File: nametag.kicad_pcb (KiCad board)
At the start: 2 copper layers, 180 x 54 mm, 116 parts, among them P1 ISP, Q1 2N7002, Q2 2N7002, Q3 2N7002, Q4 2N7002, Q5 2N7002, U1 ATTINY13-SS

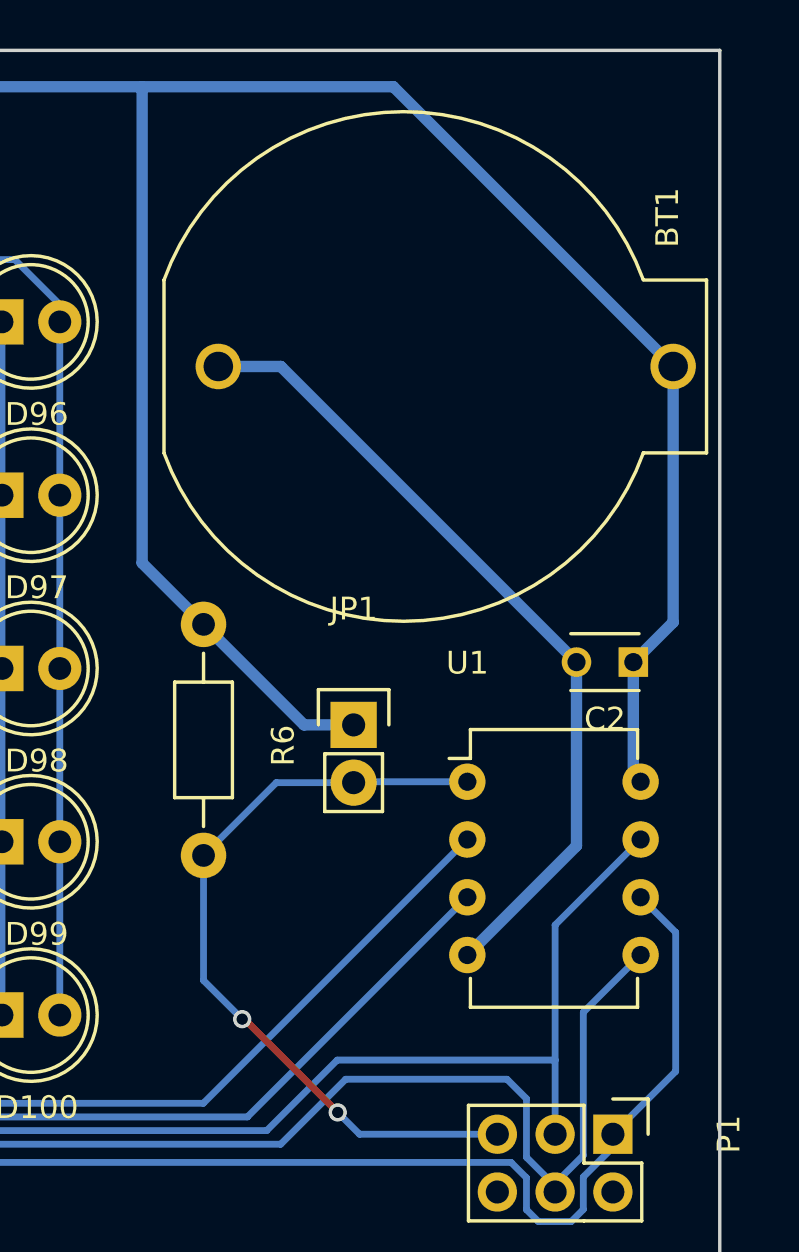
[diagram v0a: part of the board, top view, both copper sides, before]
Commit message: Improved ground plane area
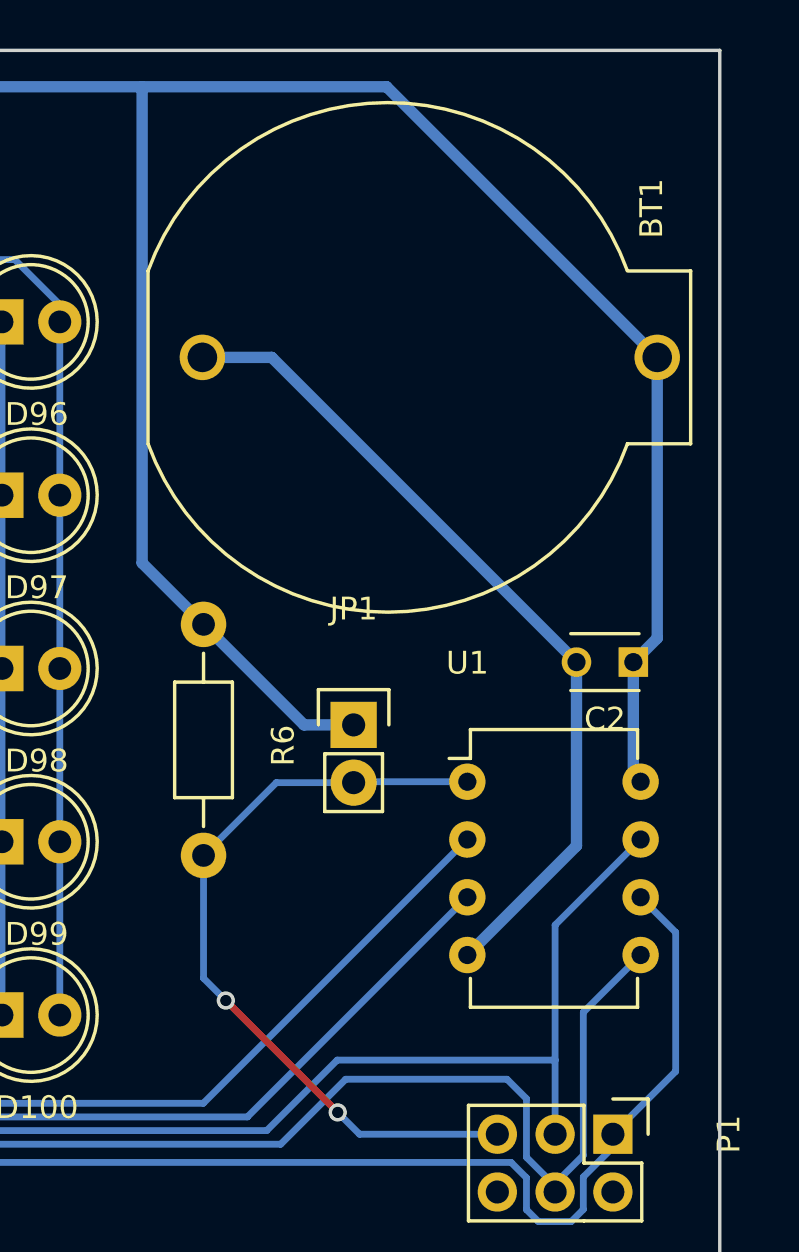
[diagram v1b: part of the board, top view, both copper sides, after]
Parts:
- moved BT1 0.81 mm to (225.4, 73.5)
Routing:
- net GND: track 36.0 -> 36.9 mm
- net VCC: track 236.2 -> 235.4 mm
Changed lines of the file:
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@@
   )
   (module nametag:CR2032 (layer F.Cu)
-    (at 226.1 73.9)
+    (at 225.4 73.5)
     (descr "CR2032 coin battery holder (PTH)")
     (tags "battery holder cr2032")
@@
   (gr_line (start 60 114) (end 240 114) (layer Edge.Cuts) (width 0.15))
   (gr_line (start 60 60) (end 60 114) (layer Edge.Cuts) (width 0.15))
+  (segment (start 236.2 86.9) (end 237.25 85.85) (width 0.5) (layer B.Cu) (net 1))
+  (segment (start 237.25 85.85) (end 237.25 73.5) (width 0.5) (layer B.Cu) (net 1))
+  (segment (start 237.25 73.5) (end 225.35 61.6) (width 0.5) (layer B.Cu) (net 1))
+  (segment (start 225.35 61.6) (end 214.6 61.6) (width 0.5) (layer B.Cu) (net 1))
   (segment (start 236.52 92.16) (end 236.2 91.84) (width 0.5) (layer B.Cu) (net 1) (status 30))
   (segment (start 236.2 91.84) (end 236.2 86.9) (width 0.5) (layer B.Cu) (net 1) (status 30))
-  (segment (start 225.65 61.6) (end 214.6 61.6) (width 0.5) (layer B.Cu) (net 1))
   (segment (start 214.6 82.54) (end 214.6 61.6) (width 0.5) (layer B.Cu) (net 1))
   (segment (start 214.6 61.6) (end 193.3 61.6) (width 0.5) (layer B.Cu) (net 1))
@@
   (segment (start 223.9 89.66) (end 221.72 89.66) (width 0.5) (layer B.Cu) (net 1) (status 10))
   (segment (start 221.72 89.66) (end 217.3 85.24) (width 0.5) (layer B.Cu) (net 1) (status 20))
-  (segment (start 236.2 86.9) (end 237.95 85.15) (width 0.5) (layer B.Cu) (net 1) (status 10))
-  (segment (start 237.95 85.15) (end 237.95 73.9) (width 0.5) (layer B.Cu) (net 1) (status 20))
-  (segment (start 237.95 73.9) (end 225.65 61.6) (width 0.5) (layer B.Cu) (net 1) (status 10))
   (segment (start 74 61.6) (end 101.8 61.6) (width 0.5) (layer B.Cu) (net 1))
   (segment (start 101.8 61.6) (end 132.3 61.6) (width 0.5) (layer B.Cu) (net 1))
@@
   (segment (start 193.2 61.7) (end 193.3 61.6) (width 0.5) (layer B.Cu) (net 1))
   (segment (start 71.28 64.32) (end 74 61.6) (width 0.5) (layer B.Cu) (net 1) (status 10))
+  (segment (start 233.7 86.9) (end 220.3 73.5) (width 0.5) (layer B.Cu) (net 2))
+  (segment (start 220.3 73.5) (end 217.25 73.5) (width 0.5) (layer B.Cu) (net 2))
   (segment (start 233.7 86.9) (end 233.7 94.98) (width 0.5) (layer B.Cu) (net 2) (status 10))
   (segment (start 233.7 94.98) (end 228.9 99.78) (width 0.5) (layer B.Cu) (net 2) (status 20))
-  (segment (start 217.95 73.9) (end 220.7 73.9) (width 0.5) (layer B.Cu) (net 2) (status 10))
-  (segment (start 220.7 73.9) (end 233.7 86.9) (width 0.5) (layer B.Cu) (net 2) (status 20))
-  (segment (start 217.3 95.4) (end 217.3 100.9) (width 0.3) (layer B.Cu) (net 3) (status 10))
-  (segment (start 217.3 100.9) (end 219 102.6) (width 0.3) (layer B.Cu) (net 3))
-  (segment (start 223.2 106.7) (end 219.1 102.6) (width 0.3) (layer F.Cu) (net 3))
-  (segment (start 219.1 102.6) (end 219 102.6) (width 0.3) (layer F.Cu) (net 3))
-  (via (at 219 102.6) (size 0.8) (drill 0.5) (layers F.Cu B.Cu) (net 3))
+  (via (at 218.279855 101.781103) (size 0.8) (drill 0.5) (layers F.Cu B.Cu) (net 3))
+  (segment (start 218.279855 101.781103) (end 217.3 100.801248) (width 0.3) (layer B.Cu) (net 3))
+  (segment (start 217.3 100.801248) (end 217.3 95.4) (width 0.3) (layer B.Cu) (net 3))
+  (segment (start 218.279855 101.781103) (end 218.281103 101.781103) (width 0.3) (layer F.Cu) (net 3))
+  (segment (start 218.281103 101.781103) (end 223.2 106.7) (width 0.3) (layer F.Cu) (net 3))
   (segment (start 230.22 107.66) (end 224.16 107.66) (width 0.3) (layer B.Cu) (net 3) (status 10))
   (segment (start 224.16 107.66) (end 223.2 106.7) (width 0.3) (layer B.Cu) (net 3))

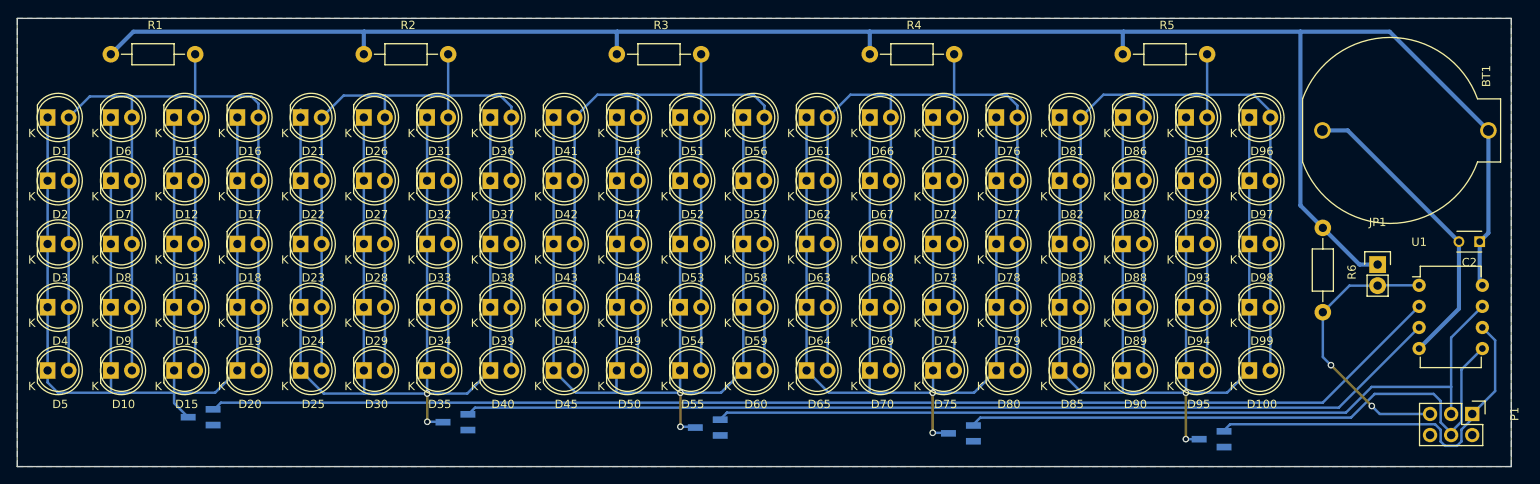
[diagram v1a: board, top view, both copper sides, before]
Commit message: Fixed reset button rail mismatch Added missing traces (GND) Replaced reset button by 4-pin standard part
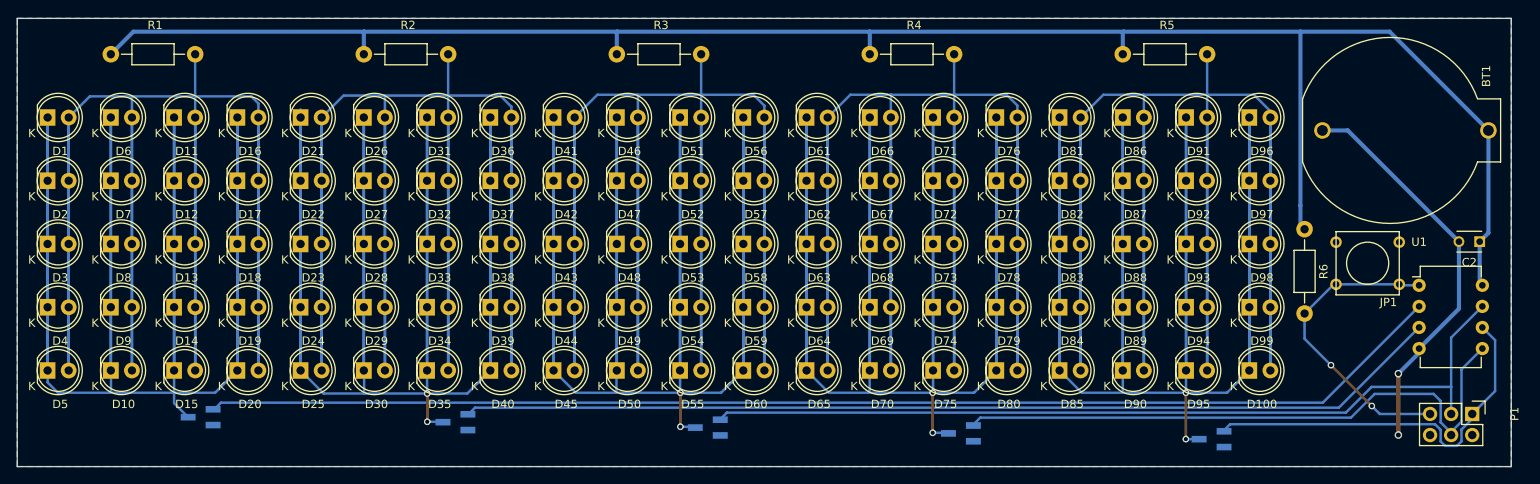
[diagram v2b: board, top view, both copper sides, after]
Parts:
- JP1: footprint Pin_Headers:Pin_Header_Straight_1x02 -> Buttons_Switches_ThroughHole:SW_PUSH_SMALL
- moved R6 2.21 mm to (215.1, 85.4)
- moved JP1 1.21 mm to (222.7, 89.5), turned to 180 degrees
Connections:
- JP1 pad 1: VCC -> /~RESET
- JP1 pad 2: /~RESET -> GND
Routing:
- net Net-(D41-Pad1): track 158.3 -> 280.3 mm
- net Net-(D21-Pad2): track 158.0 -> 279.9 mm
- net Net-(D21-Pad1): track 159.0 -> 280.9 mm
- net Net-(D100-Pad1): track 159.6 -> 281.5 mm
- net Net-(D1-Pad1): track 156.9 -> 278.8 mm
- net Net-(D100-Pad2): track 157.9 -> 279.8 mm
- net Net-(D61-Pad2): track 158.3 -> 280.2 mm
- net Net-(D61-Pad1): track 159.1 -> 281.1 mm
- net Net-(D41-Pad2): track 158.3 -> 280.2 mm
- net Net-(D1-Pad2): track 158.0 -> 280.0 mm
- net GND: track 36.9 -> 48.3 mm, vias 0 -> 2
- net VCC: track 235.4 -> 226.2 mm
- net /~RESET: track 34.1 -> 37.2 mm

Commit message: Connected Vcc to ISP header Better GND routing in layout
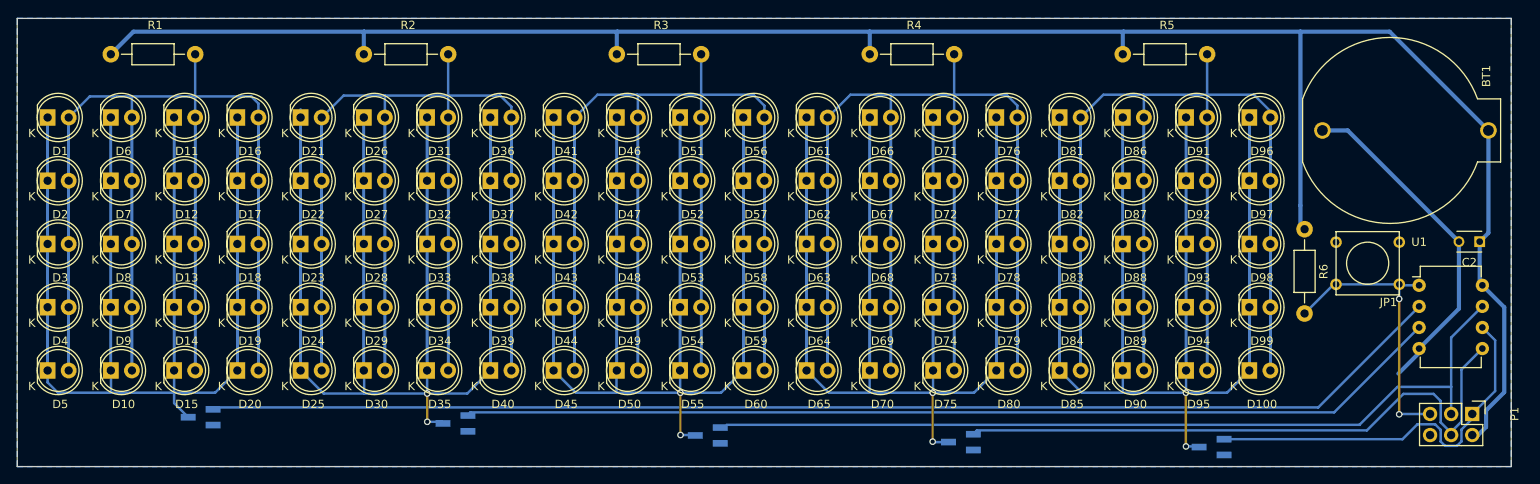
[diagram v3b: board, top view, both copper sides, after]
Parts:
- moved Q4 1.05 mm to (173.7, 111.0)
- moved Q5 0.95 mm to (203.9, 111.7)
- moved Q3 0.95 mm to (143.2, 110.2)
- moved Q2 0.15 mm to (112.8, 108.8)
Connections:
- P1 pad 2: (no net) -> VCC
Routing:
- net VCC: track 226.2 -> 247.4 mm
- net GND: track 48.3 -> 40.9 mm, vias 2 -> 0
- net /~RESET: track 37.2 -> 34.7 mm
- net Net-(D61-Pad1): track 281.1 -> 282.2 mm
- net Net-(D41-Pad1): track 280.3 -> 281.2 mm
- net Net-(D100-Pad1): track 281.5 -> 282.4 mm
- net /DIGIT3: track 74.7 -> 75.3 mm

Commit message: THT nametag: Removed Vcc jumper wire
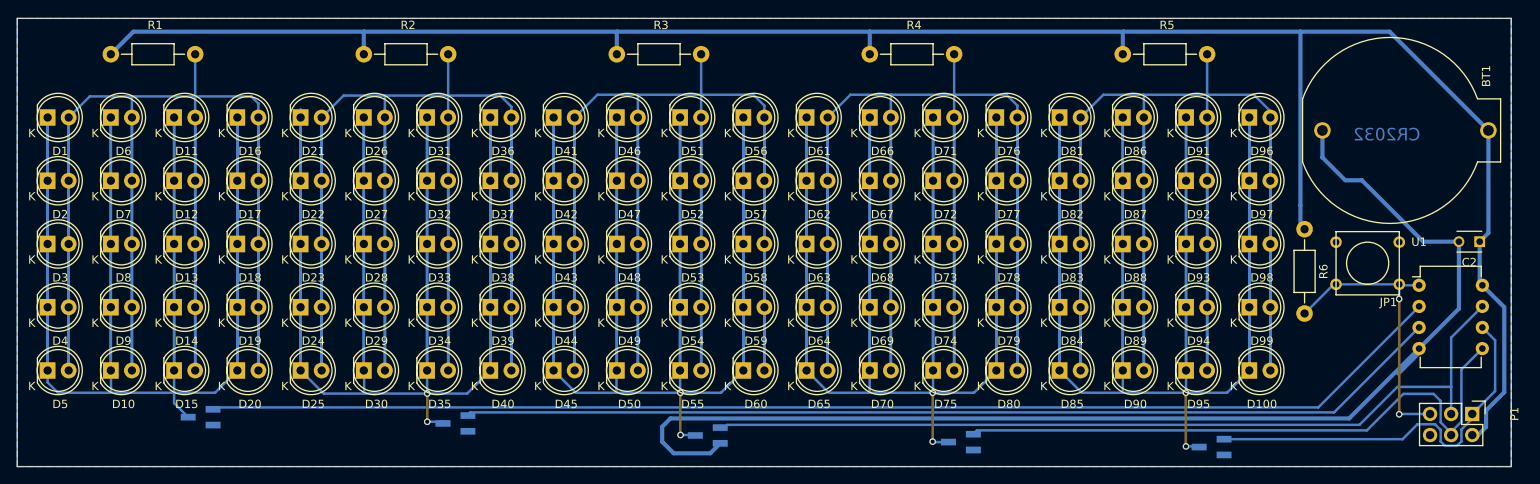
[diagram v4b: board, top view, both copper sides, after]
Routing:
- net GND: track 40.9 -> 147.8 mm
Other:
- board text added: "CR2032"
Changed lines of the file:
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@@
     (links 231)
     (no_connects 0)
-    (area 59.924999 59.69488 241.375 114.829762)
+    (area 59.924999 59.69488 252 119.200001)
     (thickness 1.6)
-    (drawings 4)
-    (tracks 407)
+    (drawings 7)
+    (tracks 417)
     (zones 0)
     (modules 116)
@@
     (last_trace_width 0.3)
     (trace_clearance 0.2)
-    (zone_clearance 0.4)
+    (zone_clearance 0.5)
     (zone_45_only no)
     (trace_min 0.2)
@@
       (net 2 GND))
   )
+  (gr_text CR2032 (at 225 74) (layer B.Cu)
+    (effects (font (size 1.5 1.5) (thickness 0.3)) (justify mirror))
+  )
+  (dimension 54 (width 0.3) (layer Dwgs.User)
+    (gr_text "54.000 mm" (at 245.35 87 90) (layer Dwgs.User)
+      (effects (font (size 1.5 1.5) (thickness 0.3)))
+    )
+    (feature1 (pts (xy 240 60) (xy 246.7 60)))
+    (feature2 (pts (xy 240 114) (xy 246.7 114)))
+    (crossbar (pts (xy 244 114) (xy 244 60)))
+    (arrow1a (pts (xy 244 60) (xy 244.586421 61.126504)))
+    (arrow1b (pts (xy 244 60) (xy 243.413579 61.126504)))
+    (arrow2a (pts (xy 244 114) (xy 244.586421 112.873496)))
+    (arrow2b (pts (xy 244 114) (xy 243.413579 112.873496)))
+  )
+  (dimension 180 (width 0.3) (layer Dwgs.User)
+    (gr_text "180.000 mm" (at 150 117.85) (layer Dwgs.User)
+      (effects (font (size 1.5 1.5) (thickness 0.3)))
+    )
+    (feature1 (pts (xy 60 114) (xy 60 119.2)))
+    (feature2 (pts (xy 240 114) (xy 240 119.2)))
+    (crossbar (pts (xy 240 116.5) (xy 60 116.5)))
+    (arrow1a (pts (xy 60 116.5) (xy 61.126504 115.913579)))
+    (arrow1b (pts (xy 60 116.5) (xy 61.126504 117.086421)))
+    (arrow2a (pts (xy 240 116.5) (xy 238.873496 115.913579)))
+    (arrow2b (pts (xy 240 116.5) (xy 238.873496 117.086421)))
+  )
   (gr_line (start 240 60) (end 60 60) (layer Edge.Cuts) (width 0.15))
   (gr_line (start 240 114) (end 240 60) (layer Edge.Cuts) (width 0.15))
@@
   (segment (start 193.2 64.32) (end 193.2 61.7) (width 0.5) (layer B.Cu) (net 1) (status 10))
   (segment (start 71.28 64.32) (end 74 61.6) (width 0.5) (layer B.Cu) (net 1) (status 10))
+  (segment (start 139.1 112.4) (end 143.50114 112.4) (width 0.5) (layer B.Cu) (net 2))
+  (segment (start 143.50114 112.4) (end 144.70114 111.2) (width 0.5) (layer B.Cu) (net 2))
+  (segment (start 137.7 111) (end 139.1 112.4) (width 0.5) (layer B.Cu) (net 2))
+  (segment (start 137.7 109.2) (end 137.7 111) (width 0.5) (layer B.Cu) (net 2))
+  (segment (start 138.7 108.2) (end 137.7 109.2) (width 0.5) (layer B.Cu) (net 2))
+  (segment (start 220.48 108.2) (end 138.7 108.2) (width 0.5) (layer B.Cu) (net 2))
+  (segment (start 228.9 99.78) (end 220.48 108.2) (width 0.5) (layer B.Cu) (net 2))
+  (segment (start 220 79.5) (end 217.25 76.75) (width 0.5) (layer B.Cu) (net 2))
+  (segment (start 217.25 76.75) (end 217.25 73.5) (width 0.5) (layer B.Cu) (net 2))
+  (segment (start 222 79.5) (end 220 79.5) (width 0.5) (layer B.Cu) (net 2))
+  (segment (start 229.4 86.9) (end 222 79.5) (width 0.5) (layer B.Cu) (net 2))
+  (segment (start 233.7 86.9) (end 229.4 86.9) (width 0.5) (layer B.Cu) (net 2))
   (segment (start 228.9 99.78) (end 228.9 100.3) (width 0.5) (layer B.Cu) (net 2))
   (segment (start 228.9 100.3) (end 226.4 102.8) (width 0.5) (layer B.Cu) (net 2))
-  (segment (start 233.7 86.9) (end 220.3 73.5) (width 0.5) (layer B.Cu) (net 2))
-  (segment (start 220.3 73.5) (end 217.25 73.5) (width 0.5) (layer B.Cu) (net 2))
   (segment (start 233.7 86.9) (end 233.7 94.98) (width 0.5) (layer B.Cu) (net 2) (status 10))
   (segment (start 233.7 94.98) (end 228.9 99.78) (width 0.5) (layer B.Cu) (net 2) (status 20))
@@
   (segment (start 238.061205 98.781205) (end 236.52 97.24) (width 0.3) (layer B.Cu) (net 18) (status 20))
   (zone (net 2) (net_name GND) (layer B.Cu) (hatch full 0.508)
-    (connect_pads yes (clearance 0.4))
-    (min_thickness 0.3)
+    (connect_pads yes (clearance 0.5))
+    (min_thickness 0.25)
     (fill yes (arc_segments 16) (thermal_gap 0.508) (thermal_bridge_width 0.508) (smoothing chamfer))
     (polygon
@@
       )
     )
+  )
+  (zone (net 0) (net_name "") (layer B.Cu) (hatch edge 0.508)
+    (connect_pads (clearance 0.4))
+    (min_thickness 0.254)
+    (keepout (tracks not_allowed) (vias not_allowed) (copperpour not_allowed))
+    (fill (arc_segments 16) (thermal_gap 0.508) (thermal_bridge_width 0.508))
+    (polygon
+      (pts
+        (xy 220 69.5) (xy 230 69.5) (xy 230 78.5) (xy 220 78.5)
+      )
+    )
